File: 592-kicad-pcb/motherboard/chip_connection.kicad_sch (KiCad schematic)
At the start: 23 parts, among them J19 Conn_01x16, J23 Conn_01x16, J24 DF40C-40DP-0.4V(51), J3 DF40C-40DP-0.4V(51), J4 Conn_01x16

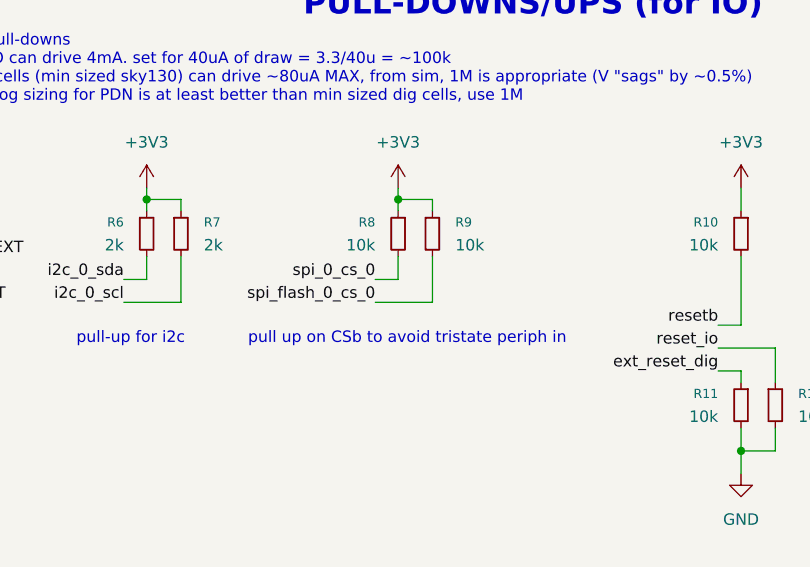
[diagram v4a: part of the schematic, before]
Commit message: add aux SPI dual-master to drive caravel CPU
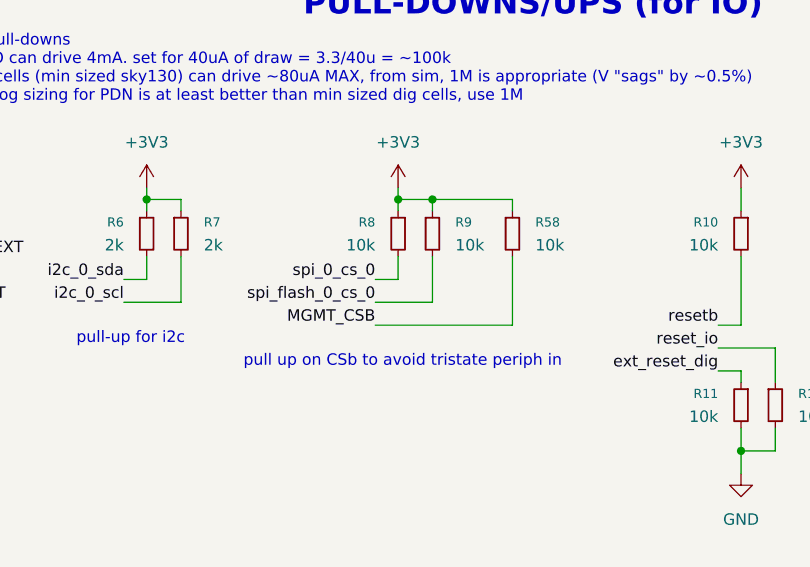
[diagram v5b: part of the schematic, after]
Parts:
- added R58: 10k, Resistor_SMD:R_0603_1608Metric, symbol Device:R_Small
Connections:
- net +3V3: now also R58.1
- net MGMT_CSB: now also R58.2
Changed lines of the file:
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@@
 	(text "pull up on CSb to avoid tristate periph in"
 		(exclude_from_sim no)
-		(at 246.126 54.864 0)
+		(at 245.618 57.404 0)
 		(effects
 			(font
@@
 	)
 	(junction
+		(at 248.92 39.37)
+		(diameter 0)
+		(color 0 0 0 0)
+	)
+	(junction
 		(at 181.61 59.69)
 		(diameter 0)
@@
 	(wire
 		(pts
+			(xy 257.81 53.34) (xy 242.57 53.34)
+		)
+		(stroke
+			(width 0)
+			(type default)
+		)
+	)
+	(wire
+		(pts
 			(xy 160.02 58.42) (xy 160.02 59.69)
 		)
@@
 	(wire
 		(pts
+			(xy 257.81 45.72) (xy 257.81 53.34)
+		)
+		(stroke
+			(width 0)
+			(type default)
+		)
+	)
+	(wire
+		(pts
 			(xy 125.73 146.05) (xy 128.27 146.05)
 		)
@@
 	(wire
 		(pts
+			(xy 257.81 40.64) (xy 257.81 39.37)
+		)
+		(stroke
+			(width 0)
+			(type default)
+		)
+	)
+	(wire
+		(pts
 			(xy 125.73 133.35) (xy 128.27 133.35)
 		)
@@
 	(wire
 		(pts
+			(xy 248.92 39.37) (xy 257.81 39.37)
+		)
+		(stroke
+			(width 0)
+			(type default)
+		)
+	)
+	(wire
+		(pts
 			(xy 287.02 64.77) (xy 287.02 67.31)
 		)
@@
 		)
 	)
+	(label "MGMT_CSB"
+		(at 242.57 53.34 180)
+		(effects
+			(font
+				(size 1.27 1.27)
+			)
+			(justify right bottom)
+		)
+	)
 	(label "i2c_0_scl"
 		(at 250.19 134.62 0)
@@
 					(unit 1)
 				)
+			)
+		)
+	)
+	(symbol
+		(lib_id "Device:R_Small")
+		(at 257.81 43.18 0)
+		(unit 1)
+		(exclude_from_sim no)
+		(in_bom yes)
+		(on_board yes)
+		(dnp no)
+		(property "Reference" "R58"
+			(at 260.35 41.9099 0)
+			(effects
+				(font
+					(size 1.016 1.016)
+				)
+				(justify left)
+			)
+		)
+		(property "Value" "10k"
+			(at 260.35 44.4499 0)
+			(effects
+				(font
+					(size 1.27 1.27)
+				)
+				(justify left)
+			)
+		)
+		(property "Footprint" "Resistor_SMD:R_0603_1608Metric"
+			(at 257.81 43.18 0)
+			(effects
+				(font
+					(size 1.27 1.27)
+				)
+				(hide yes)
+			)
+		)
+		(property "Datasheet" "~"
+			(at 257.81 43.18 0)
+			(effects
+				(font
+					(size 1.27 1.27)
+				)
+				(hide yes)
+			)
+		)
+		(property "Description" "Resistor, small symbol"
+			(at 257.81 43.18 0)
+			(effects
+				(font
+					(size 1.27 1.27)
+				)
+				(hide yes)
+			)
+		)
+		(property "LCSC" "C25804"
+			(at 257.81 43.18 0)
+			(effects
+				(font
+					(size 1.27 1.27)
+				)
+				(hide yes)
+			)
+		)
+		(property "Characteristics" ""
+			(at 257.81 43.18 0)
+			(effects
+				(font
+					(size 1.27 1.27)
+				)
+				(hide yes)
+			)
+		)
+		(property "DigikeyPN" ""
+			(at 257.81 43.18 0)
+			(effects
+				(font
+					(size 1.27 1.27)
+				)
+				(hide yes)
+			)
+		)
+		(property "MPN" ""
+			(at 257.81 43.18 0)
+			(effects
+				(font
+					(size 1.27 1.27)
+				)
+				(hide yes)
+			)
+		)
+		(property "MPN_ALT" ""
+			(at 257.81 43.18 0)
+			(effects
+				(font
+					(size 1.27 1.27)
+				)
+				(hide yes)
+			)
+		)
+		(property "Manufacturer" ""
+			(at 257.81 43.18 0)
+			(effects
+				(font
+					(size 1.27 1.27)
+				)
+				(hide yes)
+			)
+		)
+		(property "Variant" ""
+			(at 257.81 43.18 0)
+			(effects
+				(font
+					(size 1.27 1.27)
+				)
+				(hide yes)
+			)
+		)
+		(property "Vendor" ""
+			(at 257.81 43.18 0)
+			(effects
+				(font
+					(size 1.27 1.27)
+				)
+				(hide yes)
+			)
+		)
+		(pin "2"
+		)
+		(pin "1"
+		)
+		(instances
+			(project "motherboard"
+				(path "/5b0c97ac-fa03-4db8-b41b-0eee32b6f55d/f049e4ad-bebe-4338-850a-2727de737ae9/f6d635ad-dccc-4a37-acef-12f77d37e99b"
+					(reference "R58")
+					(unit 1)
+				)

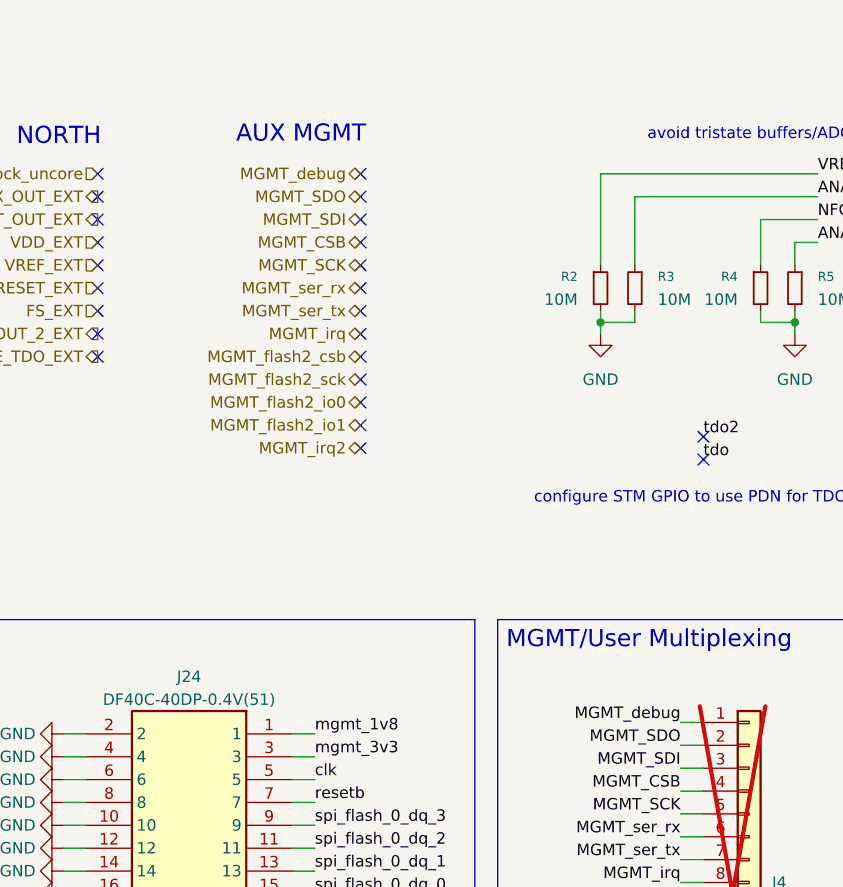
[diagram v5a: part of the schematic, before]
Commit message: map to STM pins
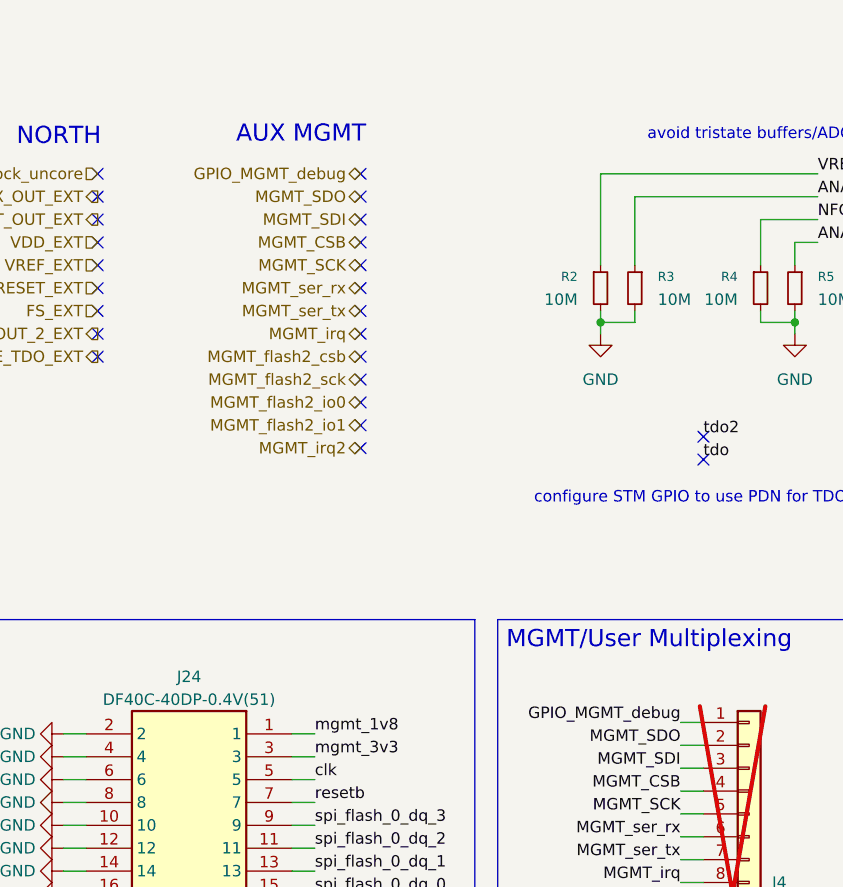
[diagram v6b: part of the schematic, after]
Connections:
- net MGMT_debug renamed GPIO_MGMT_debug
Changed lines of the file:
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@@
 		)
 	)
-	(label "MGMT_debug"
+	(label "GPIO_MGMT_debug"
 		(at 168.91 104.14 180)
 		(effects
@@
 		)
 	)
-	(hierarchical_label "MGMT_debug"
+	(hierarchical_label "GPIO_MGMT_debug"
 		(shape bidirectional)
 		(at 133.35 43.18 180)

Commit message: updates to routing
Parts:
- renumbered J24 to J4, J4 to J5, J19 to J6, J23 to J7, R58 to R10, R10 to R11, R11 to R12, R12 to R13, R13 to R14, R14 to R15, R15 to R16, R16 to R17, R17 to R18, R18 to R19, R19 to R20
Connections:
- net GND: now also J3.13; no longer J3.2
- net GPIO_MGMT_debug: now also J5.16 (Pin_16); no longer J5.1 (Pin_1)
- net MGMT_CSB: now also J5.13 (Pin_13); no longer J5.4 (Pin_4)
- net MGMT_SCK: now also J5.12 (Pin_12); no longer J5.5 (Pin_5)
- net MGMT_SDI: now also J5.14 (Pin_14); no longer J5.3 (Pin_3)
- net MGMT_SDO: now also J5.15 (Pin_15); no longer J5.2 (Pin_2)
- net MGMT_flash2_csb: now also J5.8 (Pin_8); no longer J5.9 (Pin_9)
- net MGMT_flash2_io0: now also J5.6 (Pin_6); no longer J5.11 (Pin_11)
- net MGMT_flash2_io1: now also J5.5 (Pin_5); no longer J5.12 (Pin_12)
- net MGMT_flash2_sck: now also J5.7 (Pin_7); no longer J5.10 (Pin_10)
- net MGMT_irq: now also J5.9 (Pin_9); no longer J5.8 (Pin_8)
- net MGMT_irq2: now also J5.4 (Pin_4); no longer J5.13 (Pin_13)
- net MGMT_ser_rx: now also J5.11 (Pin_11); no longer J5.6 (Pin_6)
- net MGMT_ser_tx: now also J5.10 (Pin_10); no longer J5.7 (Pin_7)
- net gpio_0_0: now also J7.7 (Pin_7); no longer J7.10 (Pin_10)
- net gpio_1_0: now also J7.6 (Pin_6); no longer J7.11 (Pin_11)
- net i2c_0_scl: now also J7.4 (Pin_4); no longer J7.13 (Pin_13)
- net i2c_0_sda: now also J7.5 (Pin_5); no longer J7.12 (Pin_12)
- net jtag_TCK: now also J7.16 (Pin_16); no longer J7.1 (Pin_1)
- net jtag_TDI: now also J7.14 (Pin_14); no longer J7.3 (Pin_3)
- net jtag_TDO: now also J7.13 (Pin_13); no longer J7.4 (Pin_4)
- net jtag_TMS: now also J7.15 (Pin_15); no longer J7.2 (Pin_2)
- net mprj_io_0: now also J6.16 (Pin_16); no longer J6.1 (Pin_1)
- net mprj_io_1: now also J6.15 (Pin_15); no longer J6.2 (Pin_2)
- net mprj_io_10: now also J6.6 (Pin_6); no longer J6.11 (Pin_11)
- net mprj_io_11: now also J6.5 (Pin_5); no longer J6.12 (Pin_12)
- net mprj_io_12: now also J6.4 (Pin_4); no longer J6.13 (Pin_13)
- net mprj_io_2: now also J6.14 (Pin_14); no longer J6.3 (Pin_3)
- net mprj_io_3: now also J6.13 (Pin_13); no longer J6.4 (Pin_4)
- net mprj_io_4: now also J6.12 (Pin_12); no longer J6.5 (Pin_5)
- net mprj_io_5: now also J6.11 (Pin_11); no longer J6.6 (Pin_6)
- net mprj_io_6: now also J6.10 (Pin_10); no longer J6.7 (Pin_7)
- net mprj_io_7: now also J6.9 (Pin_9); no longer J6.8 (Pin_8)
- net mprj_io_8: now also J6.8 (Pin_8); no longer J6.9 (Pin_9)
- net mprj_io_9: now also J6.7 (Pin_7); no longer J6.10 (Pin_10)
- net reset_io: now also J7.8 (Pin_8); no longer J7.9 (Pin_9)
- net spi_0_cs_0: now also J7.10 (Pin_10); no longer J7.7 (Pin_7)
- net spi_0_dq_0: now also J7.11 (Pin_11); no longer J7.6 (Pin_6)
- net spi_0_dq_1: now also J7.12 (Pin_12); no longer J7.5 (Pin_5)
- net spi_0_sck: now also J7.9 (Pin_9); no longer J7.8 (Pin_8)
- net user_3v3: now also J3.2; no longer J3.13
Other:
- note added: "go to 4x mux chips idea: have a single jumper that's "management mode" that handles all sources of interest"

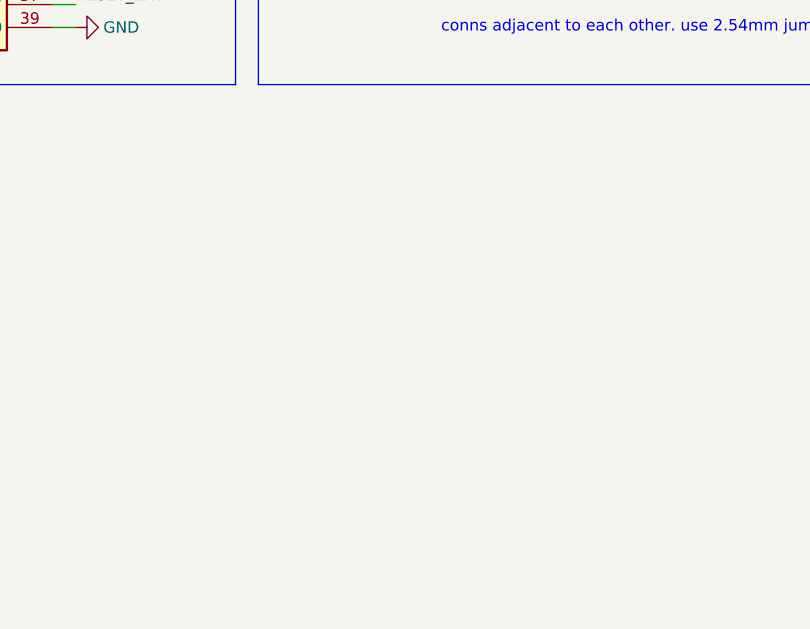
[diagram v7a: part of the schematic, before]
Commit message: more routing progress, add termination resistors
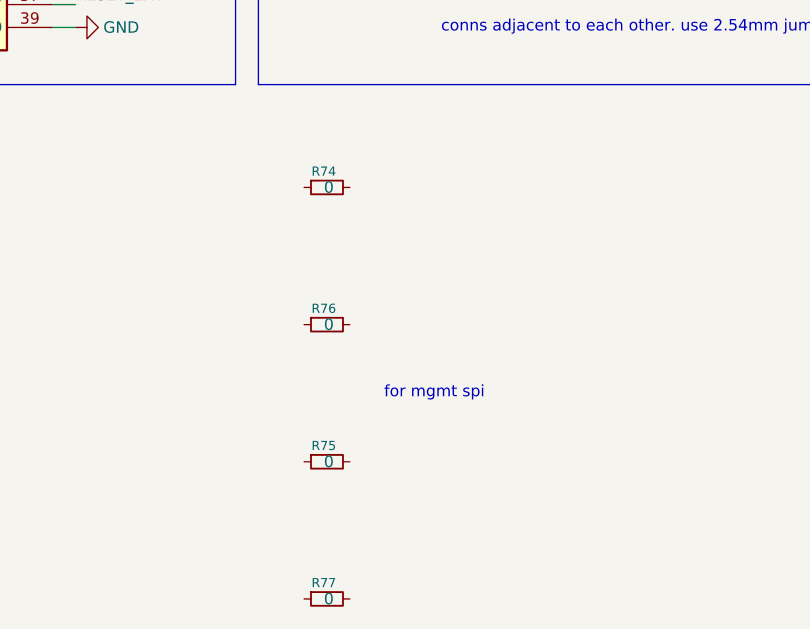
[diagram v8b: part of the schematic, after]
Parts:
- added R74, R75, R76, R77: 0, Resistor_SMD:R_0402_1005Metric, symbol Device:R_Small
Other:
- note added: "for mgmt spi"
